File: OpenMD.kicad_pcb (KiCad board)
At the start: 6 copper layers, 75 x 50 mm, 199 parts, among them IC2 RAA2118054GP3#JA0, J1 GND, J2 Digital, J3 Analog, J5 A, J6 B, J7 C, J8 V_{BATT}, Q1 EPC2302, Q2 EPC2302, Q3 EPC2302, Q4 EPC2302, Q5 EPC2302, Q6 EPC2302, U1 UP1966E, U10 INA241A2, U2 UP1966E, U3 UP1966E, U8 INA241A2, U9 INA241A2

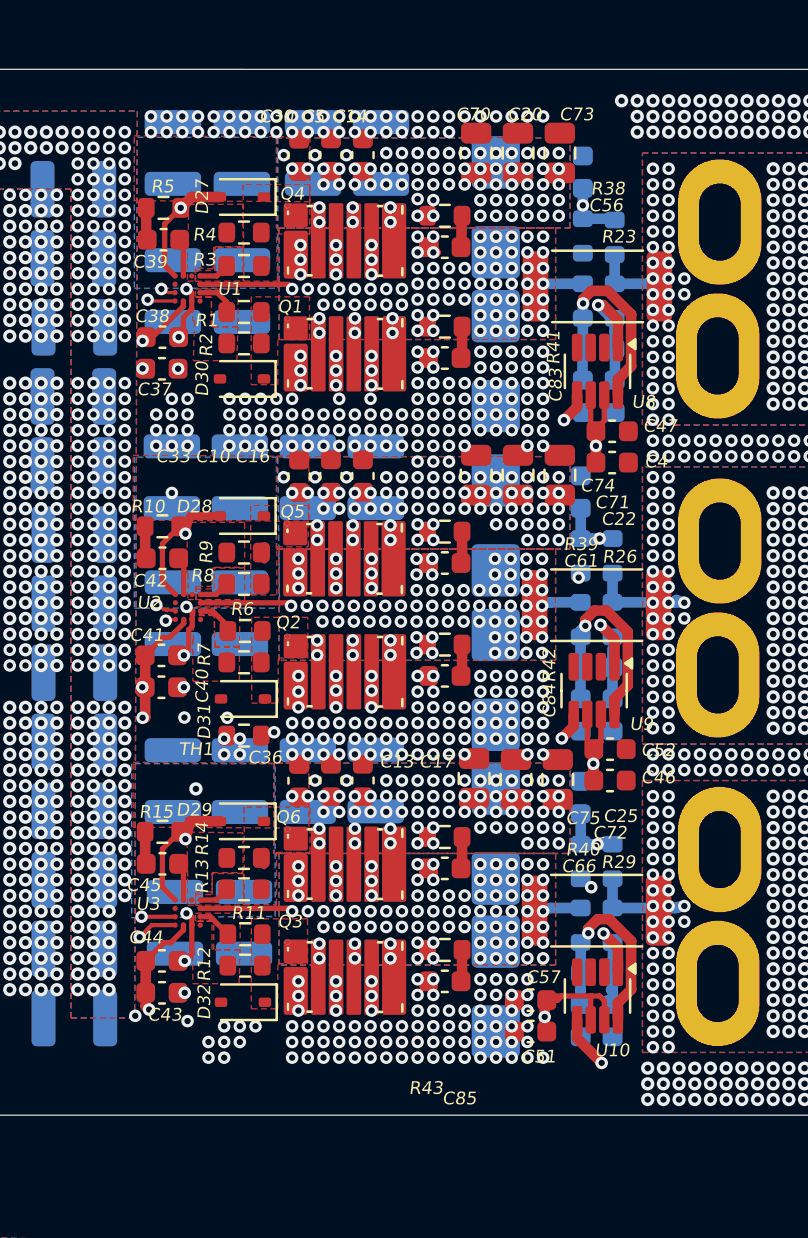
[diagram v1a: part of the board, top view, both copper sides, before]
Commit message: moved amps to back
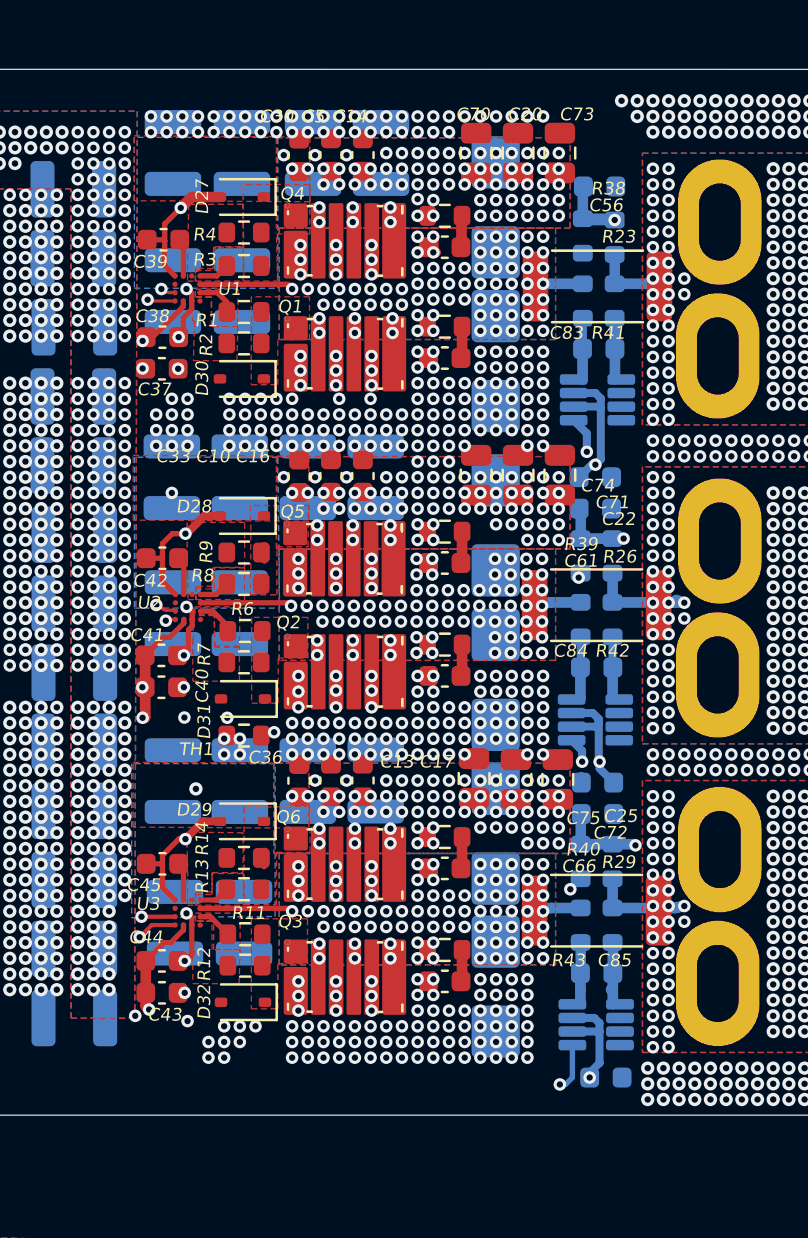
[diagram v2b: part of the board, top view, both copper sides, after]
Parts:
- removed C4, C46, C51: 4.7uF, Capacitor_SMD:C_0603_1608Metric
- removed C48, C50, C53, C55, C58, C60: 100nF, Capacitor_SMD:C_0603_1608Metric
- removed R10, R15, R5: 0, Resistor_SMD:R_0603_1608Metric
- C12, C15, C18, C19, C2, C21, C23, C24, C26, C27, C28, C29, C3, C31, C32, C34, C35, C6, C7, C78, C79, C8, C80, C81, C82, C86, C87, C88, C89, C9, C91: value 4.7uF -> 10uF
- C47, C52, C57, U10, U8, U9: moved to B.Cu
- D11, D21, D22, D23, D7, D8, D9: value 3.6V -> 3.3V
- moved C57 5.16 mm to (149.4, 125.5), turned to 0 degrees
- moved C47 2.34 mm to (148.9, 96.8)
- moved C52 1.71 mm to (149.0, 111.4), turned to 180 degrees
- moved U9 1.40 mm to (148.9, 108.4), turned to 180 degrees
- moved U10 1.38 mm to (148.9, 123.0), turned to 180 degrees
- moved U8 1.36 mm to (149.0, 93.1), turned to 180 degrees
- moved C69 1.13 mm to (149.0, 112.9), turned to 0 degrees
- moved C68 1.06 mm to (148.9, 98.3), turned to 0 degrees
- moved C67 1.05 mm to (149.1, 82.9), turned to 0 degrees
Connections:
- C39 pad 2: /Predrivers/Gate Driver A/SW -> /SW.A
- C42 pad 2: /Predrivers/Gate Driver B/SW -> /SW.B
- C45 pad 2: /Predrivers/Gate Driver C/SW -> /SW.C
- C56 pad 2: /DRV.A -> /SW.A
- C61 pad 2: /DRV.B -> /SW.B
- C66 pad 2: /DRV.C -> /SW.C
- D1 pad 2: /DRV.A -> /SW.A
- D2 pad 1: /DRV.A -> /SW.A
- D27 pad 2: /DRV.A -> /SW.A
- D28 pad 2: /DRV.B -> /SW.B
- D29 pad 2: /DRV.C -> /SW.C
- D3 pad 2: /DRV.B -> /SW.B
- D4 pad 1: /DRV.B -> /SW.B
- D5 pad 2: /DRV.C -> /SW.C
- D6 pad 1: /DRV.C -> /SW.C
- Q1 pad 3: /DRV.A -> /SW.A
- Q1 pad 5: /DRV.A -> /SW.A
- Q1 pad 7: /DRV.A -> /SW.A
- Q2 pad 3: /DRV.B -> /SW.B
- Q2 pad 5: /DRV.B -> /SW.B
- Q2 pad 7: /DRV.B -> /SW.B
- Q3 pad 3: /DRV.C -> /SW.C
- Q3 pad 5: /DRV.C -> /SW.C
- Q3 pad 7: /DRV.C -> /SW.C
- Q4 pad 2: /DRV.A -> /SW.A
- Q4 pad 4: /DRV.A -> /SW.A
- Q4 pad 6: /DRV.A -> /SW.A
- Q5 pad 2: /DRV.B -> /SW.B
- Q5 pad 4: /DRV.B -> /SW.B
- Q5 pad 6: /DRV.B -> /SW.B
- Q6 pad 2: /DRV.C -> /SW.C
- Q6 pad 4: /DRV.C -> /SW.C
- Q6 pad 6: /DRV.C -> /SW.C
- R22 pad 1: /DRV.A -> /SW.A
- R23 pad 1: /DRV.A -> /SW.A
- R25 pad 1: /DRV.B -> /SW.B
- R26 pad 1: /DRV.B -> /SW.B
- R28 pad 1: /DRV.C -> /SW.C
- R29 pad 1: /DRV.C -> /SW.C
- R41 pad 1: /DRV.A -> /SW.A
- R42 pad 1: /DRV.B -> /SW.B
- R43 pad 1: /DRV.C -> /SW.C
- U1 pad C1: /DRV.A -> /SW.A
- U1 pad D4: /DRV.A -> /SW.A
- U2 pad C1: /DRV.B -> /SW.B
- U2 pad D4: /DRV.B -> /SW.B
- U3 pad C1: /DRV.C -> /SW.C
- U3 pad D4: /DRV.C -> /SW.C
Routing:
- net /SW.A: track 0.00 -> 14.6 mm, vias 0 -> 85
- net /DRV.A: track 13.7 -> 0.00 mm, vias 85 -> 0
- net /DRV.C: track 12.9 -> 0.00 mm, vias 85 -> 0
- net /SW.B: track 0.00 -> 12.9 mm, vias 0 -> 81
- net /SW.C: track 0.00 -> 12.9 mm, vias 0 -> 85
- net /DRV.B: track 12.7 -> 0.00 mm, vias 81 -> 0
- net /Phase Current Sensors/Current Sense A/V+: track 10.9 -> 2.93 mm, vias 1 -> 0
- net /Phase Current Sensors/Current Sense B/V+: track 10.7 -> 2.93 mm, vias 1 -> 0
- net /Phase Current Sensors/Current Sense C/V+: track 9.80 -> 2.89 mm, vias 1 -> 0
- net /Phase Current Sensors/Current Sense A/V-: track 6.28 -> 2.90 mm, vias 1 -> 0
- net /Phase Current Sensors/Current Sense B/V-: track 5.99 -> 2.93 mm, vias 1 -> 0
- net /V_SENSE.A: track 61.8 -> 64.7 mm
- net /I_SENSE.B: track 97.4 -> 94.5 mm
- net /I_SENSE.C: track 80.8 -> 78.1 mm
- net /Phase Current Sensors/Current Sense C/V-: track 5.72 -> 2.98 mm, vias 1 -> 0
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- added copper zone on B.Cu, net /SW.A
- added copper zone on F.Cu, net /SW.A
- added copper zone on In1.Cu, net /SW.A
- added copper zone on In2.Cu, net /SW.A
- added copper zone on In3.Cu, net /SW.A
- added copper zone on In4.Cu, net /SW.A
- added copper zone on B.Cu, net /SW.B
- added copper zone on F.Cu, net /SW.B
- added copper zone on In1.Cu, net /SW.B
- added copper zone on In2.Cu, net /SW.B
- added copper zone on In3.Cu, net /SW.B
- added copper zone on In4.Cu, net /SW.B
- added copper zone on B.Cu, net /SW.C
- added copper zone on F.Cu, net /SW.C
- added copper zone on In1.Cu, net /SW.C
- added copper zone on In2.Cu, net /SW.C
- added copper zone on In3.Cu, net /SW.C
- added copper zone on In4.Cu, net /SW.C
- removed copper zone on B.Cu, net /DRV.A
- removed copper zone on F.Cu, net /DRV.A
- removed copper zone on In1.Cu, net /DRV.A
- removed copper zone on In2.Cu, net /DRV.A
- removed copper zone on In3.Cu, net /DRV.A
- removed copper zone on In4.Cu, net /DRV.A
- removed copper zone on B.Cu, net /DRV.B
- removed copper zone on F.Cu, net /DRV.B
- removed copper zone on In1.Cu, net /DRV.B
- removed copper zone on In2.Cu, net /DRV.B
- removed copper zone on In3.Cu, net /DRV.B
- removed copper zone on In4.Cu, net /DRV.B
- removed copper zone on B.Cu, net /DRV.C
- removed copper zone on F.Cu, net /DRV.C
- removed copper zone on In1.Cu, net /DRV.C
- removed copper zone on In2.Cu, net /DRV.C
- removed copper zone on In3.Cu, net /DRV.C
- removed copper zone on In4.Cu, net /DRV.C

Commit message: fixed grounding issues
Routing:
- net /DRV_TEMP_SENSE: track 87.1 -> 84.4 mm
- net /V_{DRV}: track 68.8 -> 70.1 mm, vias 6 -> 5
- net /V_{BATT}: vias 591 -> 587
- net /GND: vias 1079 -> 1085
- added copper zone on In4.Cu, net /GND
